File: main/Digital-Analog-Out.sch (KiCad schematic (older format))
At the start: 10 parts, among them IC1 PCM1780DBQ, J2 AudioJack3

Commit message: Add DAC footprint
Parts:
- IC1: footprint SOP64P600X175-16N -> DAC:SOP64P600X175-16N
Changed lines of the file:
@@
 F 0 "IC1" H 5800 4065 50  0000 C CNN
 F 1 "PCM1780DBQ" H 5800 3974 50  0000 C CNN
-F 2 "SOP64P600X175-16N" H 6500 3900 50  0001 L CNN
+F 2 "DAC:SOP64P600X175-16N" H 6500 3900 50  0001 L CNN
 F 3 "http://www.ti.com/lit/gpn/pcm1780" H 6500 3800 50  0001 L CNN
 F 4 "PCM1780DBQ, Audio DAC Octal 24 bit-, 192ksps Serial, 16-Pin SSOP" H 6500 3700 50  0001 L CNN "Description"

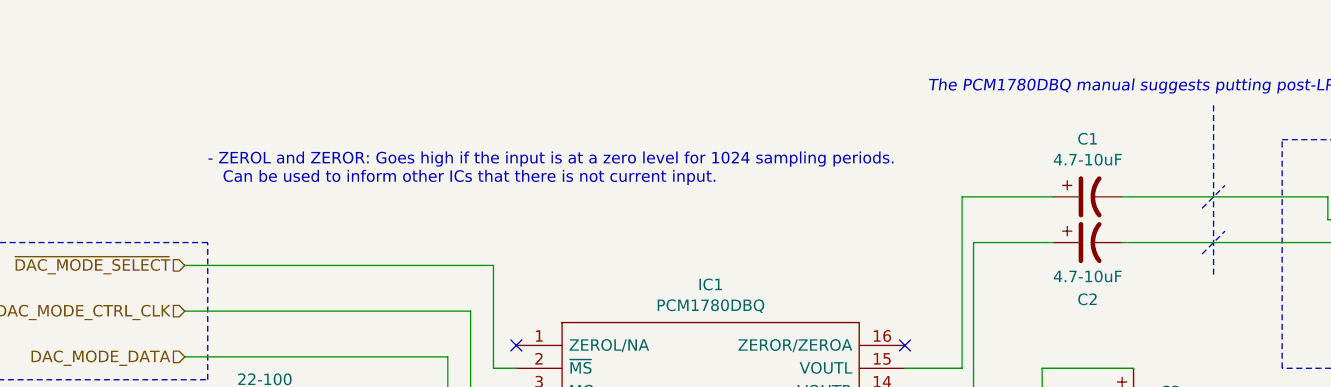
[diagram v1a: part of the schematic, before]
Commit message: Move EFM32GG debug port inside MCU sheet
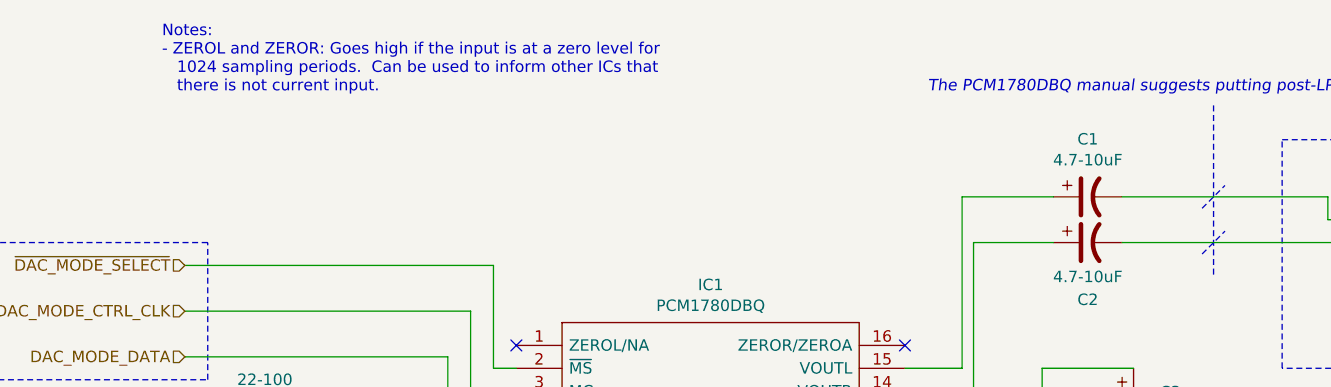
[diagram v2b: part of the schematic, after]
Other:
- note added: "Notes:\n- ZEROL and ZEROR: Goes high if the input is at a zero level for\n 1024 sampling periods. Can be used to inform other ICs that\n there is not current input."
- note removed: "- ZEROL and ZEROR: Goes high if the input is at a zero level for 1024 sampling periods. \n Can be used to inform other ICs that there is not current input."
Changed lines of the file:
@@
 	0    1    1    0
 $EndComp
-Text Notes 3600 3100 0    50   ~ 0
-- ZEROL and ZEROR: Goes high if the input is at a zero level for 1024 sampling periods. \n   Can be used to inform other ICs that there is not current input.
+Text Notes 3400 2700 0    50   ~ 0
+Notes:\n- ZEROL and ZEROR: Goes high if the input is at a zero level for\n   1024 sampling periods.  Can be used to inform other ICs that\n   there is not current input.
 NoConn ~ 4950 3800
 NoConn ~ 6650 3800

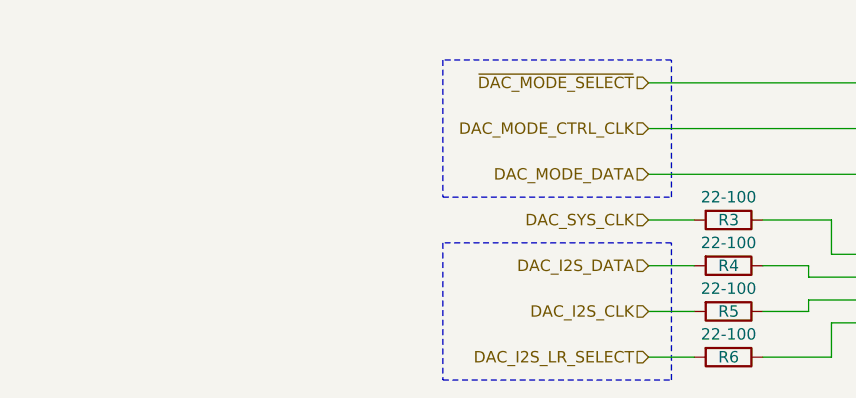
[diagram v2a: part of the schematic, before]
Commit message: Simplify the top sheet, put bus connection inside the sheets
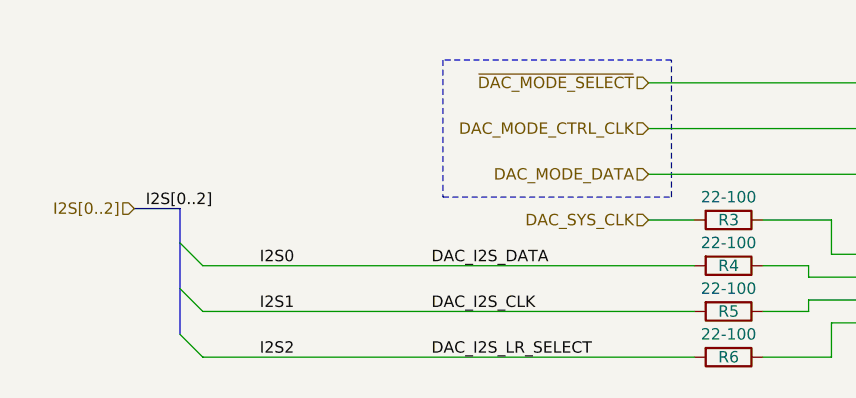
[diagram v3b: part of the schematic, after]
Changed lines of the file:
@@
 Text HLabel 3500 4050 0    50   Input ~ 0
 DAC_SYS_CLK
-Text HLabel 3500 4250 0    50   Input ~ 0
-DAC_I2S_DATA
-Text HLabel 3500 4450 0    50   Input ~ 0
-DAC_I2S_CLK
-Text HLabel 3500 4650 0    50   Input ~ 0
-DAC_I2S_LR_SELECT
-Wire Wire Line
-	3500 4650 3700 4650
-Wire Wire Line
-	3500 4450 3700 4450
-Wire Wire Line
-	3500 4250 3700 4250
 Wire Wire Line
 	3500 4050 3700 4050
@@
 Wire Notes Line
 	2600 3350 2600 3950
-Wire Notes Line
-	2600 4150 2600 4750
-Wire Notes Line
-	3600 4750 3600 4150
-Wire Notes Line
-	3600 4150 2600 4150
-Wire Notes Line
-	2600 4750 3600 4750
 Wire Wire Line
 	7600 3350 8850 3350
@@
 Wire Notes Line style solid
 	7950 3400 8050 3300
+Entry Wire Line
+	1550 4650 1450 4550
+Entry Wire Line
+	1550 4450 1450 4350
+Entry Wire Line
+	1550 4250 1450 4150
+Text Label 1300 4000 0    50   ~ 0
+I2S[0..2]
+Text Label 1950 4650 2    50   ~ 0
+I2S2
+Text Label 1950 4450 2    50   ~ 0
+I2S1
+Text Label 1950 4250 2    50   ~ 0
+I2S0
+Wire Bus Line
+	1450 4000 1250 4000
+Text HLabel 1250 4000 0    50   Input ~ 0
+I2S[0..2]
+Wire Wire Line
+	1550 4250 3700 4250
+Wire Wire Line
+	1550 4450 3700 4450
+Wire Wire Line
+	1550 4650 3700 4650
+Text Label 2550 4250 0    50   ~ 0
+DAC_I2S_DATA
+Text Label 2550 4450 0    50   ~ 0
+DAC_I2S_CLK
+Text Label 2550 4650 0    50   ~ 0
+DAC_I2S_LR_SELECT
+Wire Bus Line
+	1450 4000 1450 4550
 $EndSCHEMATC

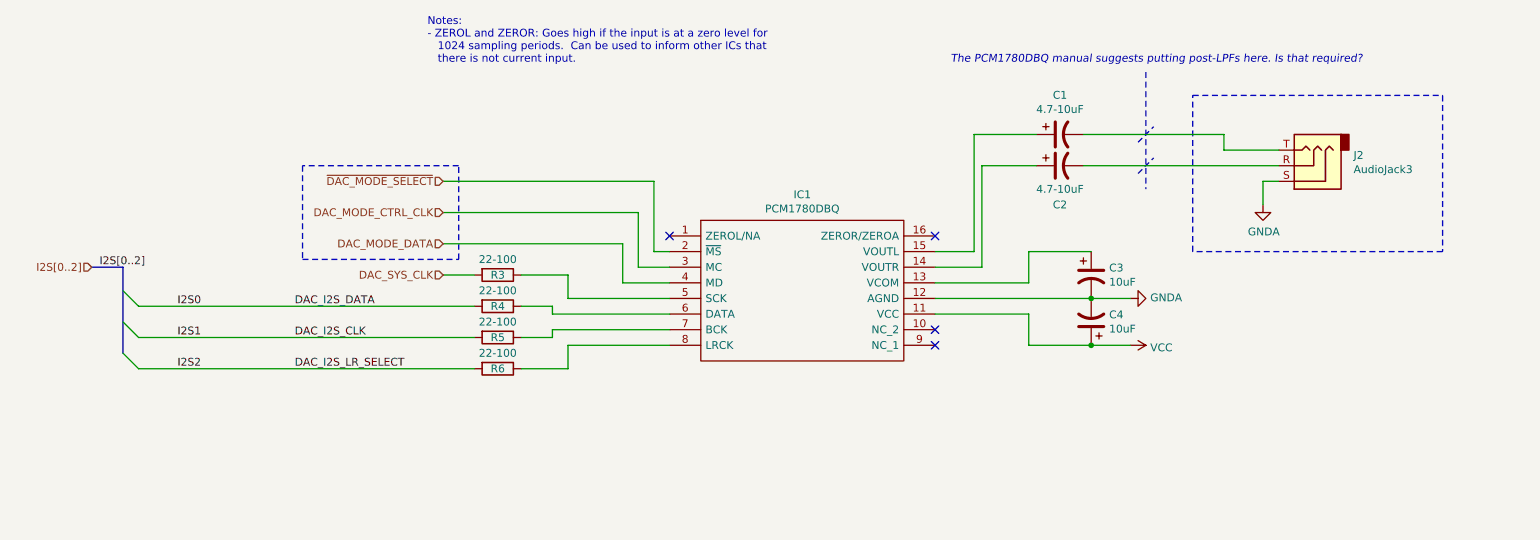
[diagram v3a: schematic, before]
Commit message: Setup FPGA power connections, connect FPGA flash
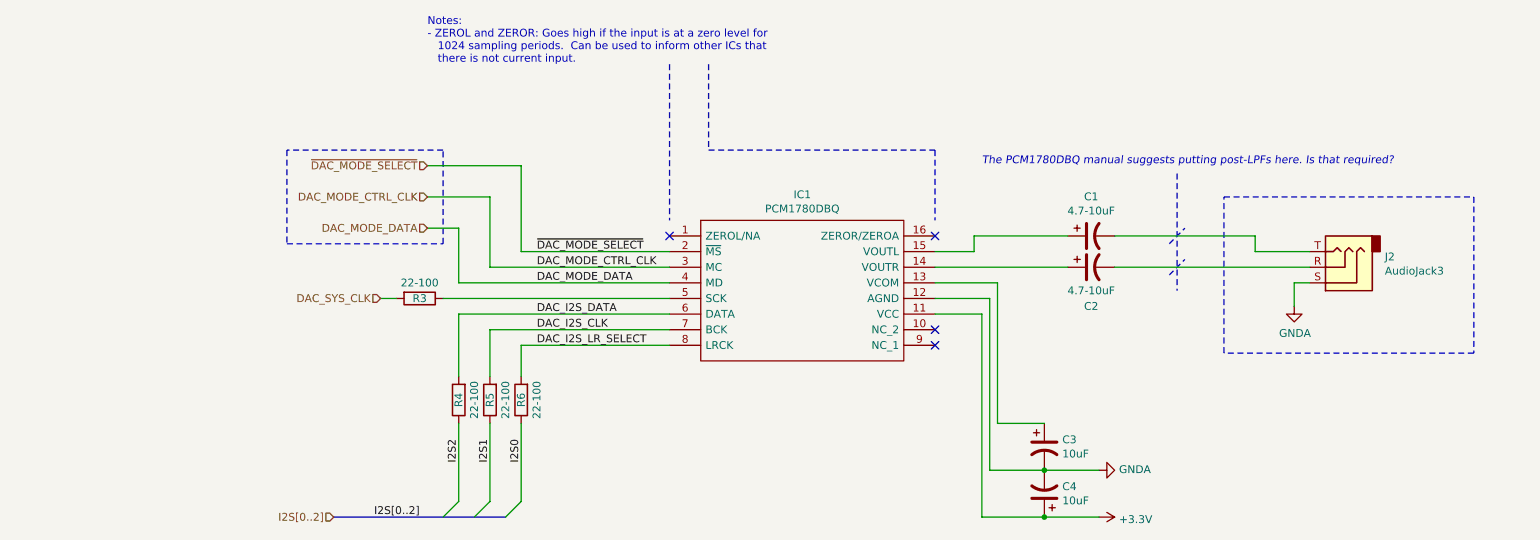
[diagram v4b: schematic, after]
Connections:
- net DAC_I2S_CLK: now also IC1.7 (BCK)
- net DAC_I2S_DATA: now also IC1.6 (DATA)
- net DAC_I2S_LR_SELECT: now also IC1.8 (LRCK)
- net I2S2: now reaches R4.1
- net I2S2: no longer IC1.6 (DATA)
- net I2S1: now reaches R5.1
- net I2S1: no longer IC1.7 (BCK)
- net I2S0: now reaches R6.1
- net I2S0: no longer IC1.8 (LRCK)
- net VCC renamed +3V3
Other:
- moved on the sheet: C1, C2, C3, C4, J2, R3, R4, R5, R6
